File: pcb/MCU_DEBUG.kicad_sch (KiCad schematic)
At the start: 1 part, among them J1 mcu_debug

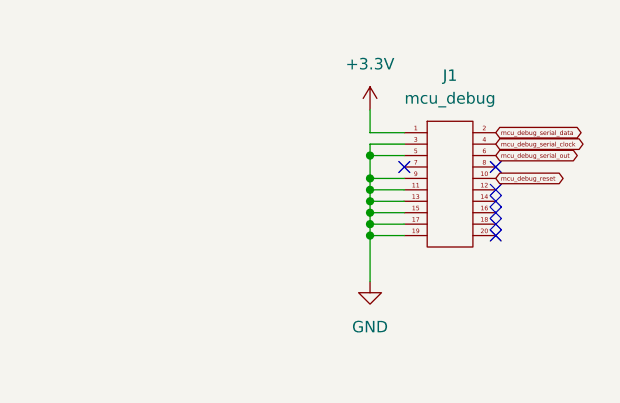
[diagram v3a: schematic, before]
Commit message: change footprint of debug_connector
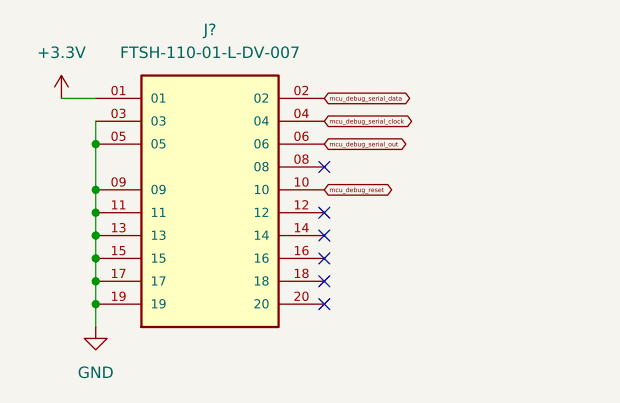
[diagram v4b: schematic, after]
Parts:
- removed J1: mcu_debug, debug-footprints:SAMTEC_FTSH-110-01-L-DV-007, symbol Carl_symboler:mcu_debug
- added J?: FTSH-110-01-L-DV-007, debug-footprints:SAMTEC_FTSH-110-01-L-DV-007, symbol debug-FTSH-110-01-L-DV-007:FTSH-110-01-L-DV-007
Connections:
- net +3.3V: now also J?.01
- net GND: now also J?.03, J?.05, J?.09, J?.11, J?.13, J?.15, J?.17, J?.19
- net mcu_debug_reset: now also J?.10
- net mcu_debug_serial_clock: now also J?.04
- net mcu_debug_serial_data: now also J?.02
- net mcu_debug_serial_out: now also J?.06
- no-connect marks 7 -> 6
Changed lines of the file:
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@@
 (kicad_sch (version 20211123) (generator eeschema)
   (paper "A4")
-  (junction (at 142.24 95.25) (diameter 0) (color 0 0 0 0)
+  (junction (at 111.76 105.41) (diameter 0) (color 0 0 0 0)
   )
-  (junction (at 142.24 93.98) (diameter 0) (color 0 0 0 0)
+  (junction (at 111.76 107.95) (diameter 0) (color 0 0 0 0)
   )
-  (junction (at 142.24 96.52) (diameter 0) (color 0 0 0 0)
+  (junction (at 111.76 102.87) (diameter 0) (color 0 0 0 0)
   )
-  (junction (at 142.24 99.06) (diameter 0) (color 0 0 0 0)
+  (junction (at 111.76 90.17) (diameter 0) (color 0 0 0 0)
   )
-  (junction (at 142.24 97.79) (diameter 0) (color 0 0 0 0)
+  (junction (at 111.76 97.79) (diameter 0) (color 0 0 0 0)
   )
-  (junction (at 142.24 100.33) (diameter 0) (color 0 0 0 0)
+  (junction (at 111.76 95.25) (diameter 0) (color 0 0 0 0)
   )
-  (junction (at 142.24 91.44) (diameter 0) (color 0 0 0 0)
+  (junction (at 111.76 100.33) (diameter 0) (color 0 0 0 0)
   )
-  (no_connect (at 156.21 96.52))
-  (no_connect (at 156.21 100.33))
-  (no_connect (at 146.05 92.71))
-  (no_connect (at 156.21 99.06))
-  (no_connect (at 156.21 97.79))
-  (no_connect (at 156.21 92.71))
-  (no_connect (at 156.21 95.25))
-  (wire (pts (xy 142.24 96.52) (xy 146.05 96.52))
+  (no_connect (at 137.16 100.33))
+  (no_connect (at 137.16 97.79))
+  (no_connect (at 137.16 107.95))
+  (no_connect (at 137.16 102.87))
+  (no_connect (at 137.16 105.41))
+  (no_connect (at 137.16 92.71))
+  (wire (pts (xy 111.76 97.79) (xy 111.76 100.33))
     (stroke (width 0) (type default) (color 0 0 0 0))
   )
-  (wire (pts (xy 142.24 97.79) (xy 142.24 99.06))
+  (wire (pts (xy 111.76 100.33) (xy 111.76 102.87))
     (stroke (width 0) (type default) (color 0 0 0 0))
   )
-  (wire (pts (xy 146.05 88.9) (xy 142.24 88.9))
+  (wire (pts (xy 111.76 95.25) (xy 111.76 97.79))
     (stroke (width 0) (type default) (color 0 0 0 0))
   )
-  (wire (pts (xy 142.24 88.9) (xy 142.24 86.36))
+  (wire (pts (xy 111.76 102.87) (xy 111.76 105.41))
     (stroke (width 0) (type default) (color 0 0 0 0))
   )
-  (wire (pts (xy 142.24 96.52) (xy 142.24 97.79))
+  (wire (pts (xy 111.76 107.95) (xy 111.76 110.49))
     (stroke (width 0) (type default) (color 0 0 0 0))
   )
-  (wire (pts (xy 142.24 95.25) (xy 146.05 95.25))
+  (wire (pts (xy 107.95 85.09) (xy 111.76 85.09))
     (stroke (width 0) (type default) (color 0 0 0 0))
   )
-  (wire (pts (xy 142.24 99.06) (xy 146.05 99.06))
+  (wire (pts (xy 111.76 90.17) (xy 111.76 95.25))
     (stroke (width 0) (type default) (color 0 0 0 0))
   )
-  (wire (pts (xy 142.24 91.44) (xy 142.24 93.98))
+  (wire (pts (xy 111.76 87.63) (xy 111.76 90.17))
     (stroke (width 0) (type default) (color 0 0 0 0))
   )
-  (wire (pts (xy 142.24 95.25) (xy 142.24 96.52))
+  (wire (pts (xy 111.76 105.41) (xy 111.76 107.95))
     (stroke (width 0) (type default) (color 0 0 0 0))
   )
-  (wire (pts (xy 142.24 99.06) (xy 142.24 100.33))
-    (stroke (width 0) (type default) (color 0 0 0 0))
-  )
-  (wire (pts (xy 142.24 90.17) (xy 142.24 91.44))
-    (stroke (width 0) (type default) (color 0 0 0 0))
-  )
-  (wire (pts (xy 142.24 93.98) (xy 142.24 95.25))
-    (stroke (width 0) (type default) (color 0 0 0 0))
-  )
-  (wire (pts (xy 142.24 93.98) (xy 146.05 93.98))
-    (stroke (width 0) (type default) (color 0 0 0 0))
-  )
-  (wire (pts (xy 142.24 91.44) (xy 146.05 91.44))
-    (stroke (width 0) (type default) (color 0 0 0 0))
-  )
-  (wire (pts (xy 142.24 97.79) (xy 146.05 97.79))
-    (stroke (width 0) (type default) (color 0 0 0 0))
-  )
-  (wire (pts (xy 142.24 100.33) (xy 146.05 100.33))
-    (stroke (width 0) (type default) (color 0 0 0 0))
-  )
-  (wire (pts (xy 146.05 90.17) (xy 142.24 90.17))
-    (stroke (width 0) (type default) (color 0 0 0 0))
-  )
-  (wire (pts (xy 142.24 100.33) (xy 142.24 105.41))
-    (stroke (width 0) (type default) (color 0 0 0 0))
-  )
-  (global_label "mcu_debug_serial_out" (shape bidirectional) (at 156.21 91.44 0) (fields_autoplaced)
+  (global_label "mcu_debug_serial_data" (shape bidirectional) (at 137.16 85.09 0) (fields_autoplaced)
     (effects (font (size 0.5 0.5)) (justify left))
-    (property "Intersheet References" "${INTERSHEET_REFS}" (id 0) (at 165.3743 91.4088 0)
+    (property "Intersheet References" "${INTERSHEET_REFS}" (id 0) (at 146.7767 85.0588 0)
       (effects (font (size 0.5 0.5)) (justify left) hide)
     )
   )
-  (global_label "mcu_debug_reset" (shape bidirectional) (at 156.21 93.98 0) (fields_autoplaced)
+  (global_label "mcu_debug_serial_clock" (shape bidirectional) (at 137.16 87.63 0) (fields_autoplaced)
     (effects (font (size 0.5 0.5)) (justify left))
-    (property "Intersheet References" "${INTERSHEET_REFS}" (id 0) (at 163.5648 93.9488 0)
+    (property "Intersheet References" "${INTERSHEET_REFS}" (id 0) (at 147.11 87.5988 0)
       (effects (font (size 0.5 0.5)) (justify left) hide)
     )
   )
-  (global_label "mcu_debug_serial_clock" (shape bidirectional) (at 156.21 90.17 0) (fields_autoplaced)
+  (global_label "mcu_debug_reset" (shape bidirectional) (at 137.16 95.25 0) (fields_autoplaced)
     (effects (font (size 0.5 0.5)) (justify left))
-    (property "Intersheet References" "${INTERSHEET_REFS}" (id 0) (at 166.16 90.1388 0)
+    (property "Intersheet References" "${INTERSHEET_REFS}" (id 0) (at 144.5148 95.2188 0)
       (effects (font (size 0.5 0.5)) (justify left) hide)
     )
   )
-  (global_label "mcu_debug_serial_data" (shape bidirectional) (at 156.21 88.9 0) (fields_autoplaced)
+  (global_label "mcu_debug_serial_out" (shape bidirectional) (at 137.16 90.17 0) (fields_autoplaced)
     (effects (font (size 0.5 0.5)) (justify left))
-    (property "Intersheet References" "${INTERSHEET_REFS}" (id 0) (at 165.8267 88.8688 0)
+    (property "Intersheet References" "${INTERSHEET_REFS}" (id 0) (at 146.3243 90.1388 0)
       (effects (font (size 0.5 0.5)) (justify left) hide)
     )
   )
-  (symbol (lib_id "Carl_symboler:mcu_debug") (at 151.13 100.33 0) (unit 1)
+  (symbol (lib_id "power:GND") (at 111.76 110.49 0) (unit 1)
     (in_bom yes) (on_board yes) (fields_autoplaced)
-    (property "Reference" "J1" (id 0) (at 151.13 82.55 0))
-    (property "Value" "mcu_debug" (id 1) (at 151.13 85.09 0))
-    (property "Footprint" "debug-footprints:SAMTEC_FTSH-110-01-L-DV-007" (id 2) (at 151.13 100.33 0)
+    (property "Reference" "#PWR0103" (id 0) (at 111.76 116.84 0)
       (effects (font (size 1.27 1.27)) hide)
     )
-    (property "Datasheet" "" (id 3) (at 151.13 100.33 0)
+    (property "Value" "GND" (id 1) (at 111.76 115.57 0))
+    (property "Footprint" "" (id 2) (at 111.76 110.49 0)
+      (effects (font (size 1.27 1.27)) hide)
+    )
+    (property "Datasheet" "" (id 3) (at 111.76 110.49 0)
       (effects (font (size 1.27 1.27)) hide)
     )
     (pin "1")
+  )
+  (symbol (lib_id "power:+3.3V") (at 107.95 85.09 0) (unit 1)
+    (in_bom yes) (on_board yes) (fields_autoplaced)
+    (property "Reference" "#PWR0102" (id 0) (at 107.95 88.9 0)
+      (effects (font (size 1.27 1.27)) hide)
+    )
+    (property "Value" "+3.3V" (id 1) (at 107.95 80.01 0))
+    (property "Footprint" "" (id 2) (at 107.95 85.09 0)
+      (effects (font (size 1.27 1.27)) hide)
+    )
+    (property "Datasheet" "" (id 3) (at 107.95 85.09 0)
+      (effects (font (size 1.27 1.27)) hide)
+    )
+    (pin "1")
+  )
+  (symbol (lib_id "debug-FTSH-110-01-L-DV-007:FTSH-110-01-L-DV-007") (at 124.46 97.79 0) (unit 1)
+    (in_bom yes) (on_board yes) (fields_autoplaced)
+    (property "Reference" "J?" (id 0) (at 124.46 77.47 0))
+    (property "Value" "FTSH-110-01-L-DV-007" (id 1) (at 124.46 80.01 0))
+    (property "Footprint" "debug-footprints:SAMTEC_FTSH-110-01-L-DV-007" (id 2) (at 124.46 97.79 0)
+      (effects (font (size 1.27 1.27)) (justify left bottom) hide)
+    )
+    (property "Datasheet" "" (id 3) (at 124.46 97.79 0)
+      (effects (font (size 1.27 1.27)) (justify left bottom) hide)
+    )
+    (property "STANDARD" "Manufacturer Recommendations" (id 4) (at 124.46 97.79 0)
+      (effects (font (size 1.27 1.27)) (justify left bottom) hide)
+    )
+    (property "MANUFACTURER" "Samtec" (id 5) (at 124.46 97.79 0)
+      (effects (font (size 1.27 1.27)) (justify left bottom) hide)
+    )
+    (property "PARTREV" "R" (id 6) (at 124.46 97.79 0)
+      (effects (font (size 1.27 1.27)) (justify left bottom) hide)
+    )
+    (pin "01")
+    (pin "02")
+    (pin "03")
+    (pin "04")
+    (pin "05")
+    (pin "06")
+    (pin "08")
+    (pin "09")
     (pin "10")
     (pin "11")
@@
     (pin "18")
     (pin "19")
-    (pin "2")
     (pin "20")
-    (pin "3")
-    (pin "4")
-    (pin "5")
-    (pin "6")
-    (pin "7")
-    (pin "8")
-    (pin "9")
-  )
-  (symbol (lib_id "power:GND") (at 142.24 105.41 0) (unit 1)
-    (in_bom yes) (on_board yes) (fields_autoplaced)
-    (property "Reference" "#PWR0103" (id 0) (at 142.24 111.76 0)
-      (effects (font (size 1.27 1.27)) hide)
-    )
-    (property "Value" "GND" (id 1) (at 142.24 110.49 0))
-    (property "Footprint" "" (id 2) (at 142.24 105.41 0)
-      (effects (font (size 1.27 1.27)) hide)
-    )
-    (property "Datasheet" "" (id 3) (at 142.24 105.41 0)
-      (effects (font (size 1.27 1.27)) hide)
-    )
-    (pin "1")
-  )
-  (symbol (lib_id "power:+3.3V") (at 142.24 86.36 0) (unit 1)
-    (in_bom yes) (on_board yes) (fields_autoplaced)
-    (property "Reference" "#PWR0102" (id 0) (at 142.24 90.17 0)
-      (effects (font (size 1.27 1.27)) hide)
-    )
-    (property "Value" "+3.3V" (id 1) (at 142.24 81.28 0))
-    (property "Footprint" "" (id 2) (at 142.24 86.36 0)
-      (effects (font (size 1.27 1.27)) hide)
-    )
-    (property "Datasheet" "" (id 3) (at 142.24 86.36 0)
-      (effects (font (size 1.27 1.27)) hide)
-    )
-    (pin "1")
   )
 )

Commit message: switch some pins for more erqonomiq layout
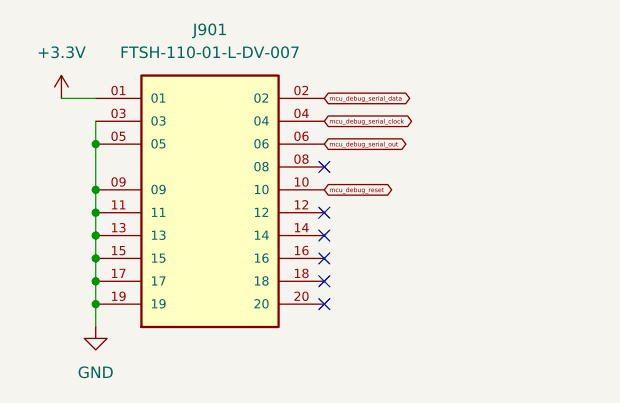
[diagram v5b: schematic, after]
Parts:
- gave numbers to parts that had none: 1
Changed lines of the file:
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@@
   (symbol (lib_id "debug-FTSH-110-01-L-DV-007:FTSH-110-01-L-DV-007") (at 124.46 97.79 0) (unit 1)
     (in_bom yes) (on_board yes) (fields_autoplaced)
-    (property "Reference" "J?" (id 0) (at 124.46 77.47 0))
+    (property "Reference" "J901" (id 0) (at 124.46 77.47 0))
     (property "Value" "FTSH-110-01-L-DV-007" (id 1) (at 124.46 80.01 0))
     (property "Footprint" "debug-footprints:SAMTEC_FTSH-110-01-L-DV-007" (id 2) (at 124.46 97.79 0)
